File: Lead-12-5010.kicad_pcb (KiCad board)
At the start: 2 copper layers, 225.5 x 42.5 mm, 59 parts, among them U1 TL082, U2 TL082

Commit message: Removed low input
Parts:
- removed D1, D2: 1N914, Diode_THT:D_DO-35_SOD27_P7.62mm_Horizontal
- removed IN_LOW_1: IN_LOW, Audio Jacks:6.35MM_STEREO_SWITCHED_JACK
- moved H2 31.0 mm to (103.9, 127.0)
- moved IN_HIGH_1 30.0 mm to (79.8, 127.3)
- moved H5 29.3 mm to (78.6, 93.1)
- moved H4 28.1 mm to (188.1, 127.0)
- moved R4 27.7 mm to (83.6, 102.9)
- moved C3 27.7 mm to (93.7, 95.2)
- moved R5 25.0 mm to (108.8, 95.2)
- moved C4 21.6 mm to (115.2, 101.6)
- moved R6 14.9 mm to (98.7, 102.9), turned to 0 degrees
- moved H1 14.0 mm to (175.3, 93.1)
- moved Logo1 11.4 mm to (172.5, 101.7)
- moved C6 10.2 mm to (161.3, 98.7)
- moved R7 2.29 mm to (121.7, 94.0)
- moved C10 1.02 mm to (174.0, 110.2)
- moved C11 1.02 mm to (165.1, 116.6)
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- renumbered OUT to OUT1, Vcc to Vcc1
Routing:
- net /V+: track 183.0 -> 131.1 mm
- net Net-(C4-Pad2): track 45.4 -> 14.6 mm
- net Net-(C3-Pad1): track 88.8 -> 62.2 mm
- net /Vref: track 234.2 -> 219.2 mm
- net Net-(C5-Pad1): track 58.4 -> 46.0 mm
- net Net-(C6-Pad2): track 42.2 -> 32.0 mm
- net Net-(C7-Pad2): track 48.0 -> 41.0 mm
- net Net-(C5-Pad2): track 28.3 -> 26.3 mm
- net Net-(C11-Pad1): track 22.5 -> 21.5 mm
- net Net-(C11-Pad2): track 60.6 -> 61.6 mm
- net Net-(IN_HIGH_1-PadT): track 11.8 -> 12.8 mm
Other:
- board size 225.5 x 42.5 mm -> 196.1 x 42.5 mm
- board text added: "v0.2"
- board text removed: "v0.1"

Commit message: Added filter cap
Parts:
- added C19: 100u/35V, Capacitor_THT:CP_Radial_D8.0mm_P3.50mm, F.Cu at (246.1, 105.0)
- C1, C2: footprint Capacitor_THT:CP_Radial_D10.0mm_P3.50mm -> Capacitor_THT:CP_Radial_D8.0mm_P3.50mm
- C16: footprint Capacitor_THT:CP_Radial_D8.0mm_P3.50mm -> Capacitor_THT:CP_Radial_D6.3mm_P2.50mm
- moved C1 5.01 mm to (255.0, 100.3)
- moved C2 2.39 mm to (263.9, 105.0)
- moved C16 2.01 mm to (238.6, 100.3)
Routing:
- net Net-(C19-Pad1): track 14.2 -> 37.1 mm
- net /Vref: track 219.2 -> 224.0 mm
- net Net-(C16-Pad2): track 30.4 -> 33.2 mm
- net /V+: track 131.1 -> 132.6 mm
- net Net-(BOOST1-Pad2): track 51.0 -> 51.7 mm

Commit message: Preparing 0.2
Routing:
- net Net-(C19-Pad1): track 37.1 -> 37.7 mm
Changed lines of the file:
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@@
     (thickness 1.6)
     (drawings 9)
-    (tracks 284)
+    (tracks 289)
     (zones 0)
     (modules 57)
@@
   (segment (start 131.572 116.84) (end 132.461 115.951) (width 1) (layer F.Cu) (net 9))
   (segment (start 132.461 115.951) (end 139.573 115.951) (width 1) (layer F.Cu) (net 9))
-  (segment (start 263.906 105.029) (end 263.906 99.441) (width 1) (layer F.Cu) (net 9) (status 1000000))
-  (segment (start 263.906 99.441) (end 260.985 96.52) (width 1) (layer F.Cu) (net 9) (status 1000000))
-  (segment (start 260.985 96.52) (end 257.27 96.52) (width 1) (layer F.Cu) (net 9) (status 1000000))
-  (segment (start 257.27 96.52) (end 253.714 92.964) (width 1) (layer F.Cu) (net 9) (status 1000000))
-  (segment (start 253.714 92.964) (end 250.19 92.964) (width 1) (layer F.Cu) (net 9) (status 1000020))
+  (segment (start 263.906 105.029) (end 263.906 99.441) (width 1) (layer F.Cu) (net 9))
+  (segment (start 263.906 99.441) (end 260.985 96.52) (width 1) (layer F.Cu) (net 9))
+  (segment (start 260.985 96.52) (end 257.27 96.52) (width 1) (layer F.Cu) (net 9))
+  (segment (start 257.27 96.52) (end 253.714 92.964) (width 1) (layer F.Cu) (net 9))
+  (segment (start 253.714 92.964) (end 250.19 92.964) (width 1) (layer F.Cu) (net 9) (status 20))
   (segment (start 220.853 90.678) (end 220.853 92.964) (width 1) (layer F.Cu) (net 10) (status 20))
   (segment (start 220.10001 89.92501) (end 220.853 90.678) (width 1) (layer F.Cu) (net 10))
@@
   (segment (start 222.758 101.346) (end 211.709 101.346) (width 0.5) (layer B.Cu) (net 15))
   (segment (start 211.709 101.346) (end 206.502 106.553) (width 0.5) (layer B.Cu) (net 15))
-  (segment (start 229.997 102.235) (end 231.394 103.632) (width 0.5) (layer F.Cu) (net 15) (status 1000000))
-  (segment (start 229.997 101.092) (end 229.997 102.235) (width 0.5) (layer F.Cu) (net 15) (status 1000000))
-  (segment (start 231.394 103.632) (end 237.236 103.632) (width 0.5) (layer F.Cu) (net 15) (status 1000000))
-  (segment (start 237.236 103.632) (end 238.633 102.235) (width 0.5) (layer F.Cu) (net 15) (status 1000000))
-  (segment (start 238.633 102.235) (end 238.633 100.33) (width 0.5) (layer F.Cu) (net 15) (status 1000000))
+  (segment (start 229.997 102.235) (end 231.394 103.632) (width 0.5) (layer F.Cu) (net 15))
+  (segment (start 229.997 101.092) (end 229.997 102.235) (width 0.5) (layer F.Cu) (net 15))
+  (segment (start 231.394 103.632) (end 237.236 103.632) (width 0.5) (layer F.Cu) (net 15))
+  (segment (start 237.236 103.632) (end 238.633 102.235) (width 0.5) (layer F.Cu) (net 15))
+  (segment (start 238.633 102.235) (end 238.633 100.33) (width 0.5) (layer F.Cu) (net 15))
   (segment (start 151.21 97.79) (end 152.4 96.6) (width 0.5) (layer F.Cu) (net 16) (status 20))
   (segment (start 144.78 97.79) (end 151.21 97.79) (width 0.5) (layer F.Cu) (net 16) (status 10))
@@
   (segment (start 234.9 128.524) (end 236.069999 127.354001) (width 0.5) (layer F.Cu) (net 21) (status 10))
   (segment (start 236.069999 127.354001) (end 236.119999 127.354001) (width 0.5) (layer F.Cu) (net 21))
-  (segment (start 237.871 111.252) (end 237.871 107.696) (width 0.5) (layer B.Cu) (net 21) (status 1000000))
-  (segment (start 240.792 114.173) (end 237.871 111.252) (width 0.5) (layer B.Cu) (net 21) (status 1000000))
-  (segment (start 240.792 119.38) (end 240.792 114.173) (width 0.5) (layer B.Cu) (net 21) (status 1000010))
-  (segment (start 241.133 104.434) (end 237.871 107.696) (width 0.5) (layer B.Cu) (net 21) (status 1000000))
-  (segment (start 241.133 100.33) (end 241.133 104.434) (width 0.5) (layer B.Cu) (net 21) (status 1000000))
+  (segment (start 237.871 111.252) (end 237.871 107.696) (width 0.5) (layer B.Cu) (net 21))
+  (segment (start 240.792 114.173) (end 237.871 111.252) (width 0.5) (layer B.Cu) (net 21))
+  (segment (start 240.792 119.38) (end 240.792 114.173) (width 0.5) (layer B.Cu) (net 21) (status 10))
+  (segment (start 241.133 104.434) (end 237.871 107.696) (width 0.5) (layer B.Cu) (net 21))
+  (segment (start 241.133 100.33) (end 241.133 104.434) (width 0.5) (layer B.Cu) (net 21))
   (segment (start 93.137999 94.450001) (end 93.137999 94.441001) (width 0.5) (layer F.Cu) (net 22) (status 10))
   (segment (start 92.338 95.25) (end 93.137999 94.450001) (width 0.5) (layer F.Cu) (net 22) (status 20))
@@
   (segment (start 229.9 128.524) (end 229.9 124.938) (width 0.5) (layer F.Cu) (net 29) (status 10))
   (segment (start 229.9 124.938) (end 239.522 115.316) (width 0.5) (layer F.Cu) (net 29))
-  (segment (start 225.806 92.964) (end 231.013 92.964) (width 1) (layer F.Cu) (net 32) (status 20))
-  (segment (start 219.456 99.314) (end 225.806 92.964) (width 1) (layer F.Cu) (net 32) (status 10))
   (segment (start 210.121 103.314) (end 202.946 96.139) (width 1) (layer F.Cu) (net 30))
-  (segment (start 202.946 92.075) (end 200.79601 89.92501) (width 1) (layer F.Cu) (net 30))
-  (segment (start 202.946 96.139) (end 202.946 92.075) (width 1) (layer F.Cu) (net 30))
-  (segment (start 150.10499 89.92501) (end 144.78 95.25) (width 1) (layer F.Cu) (net 30) (status 20))
-  (segment (start 200.79601 89.92501) (end 150.10499 89.92501) (width 1) (layer F.Cu) (net 30))
   (segment (start 220.455999 102.314001) (end 220.455999 101.870001) (width 1) (layer F.Cu) (net 30))
   (segment (start 219.456 103.314) (end 220.455999 102.314001) (width 1) (layer F.Cu) (net 30) (status 10))
@@
   (segment (start 219.456 103.314) (end 217.234 103.314) (width 1) (layer F.Cu) (net 30) (status 10))
   (segment (start 217.234 103.314) (end 210.121 103.314) (width 1) (layer F.Cu) (net 30))
-  (segment (start 240.284 92.964) (end 243.078 95.758) (width 1) (layer B.Cu) (net 30) (status 1000000))
-  (segment (start 243.078 95.758) (end 250.063 95.758) (width 1) (layer B.Cu) (net 30) (status 1000000))
-  (segment (start 250.063 95.758) (end 254.635 100.33) (width 1) (layer B.Cu) (net 30) (status 1000000))
-  (segment (start 236.093 92.964) (end 240.284 92.964) (width 1) (layer B.Cu) (net 30) (status 1000000))
-  (segment (start 254.635 100.33) (end 255.016 100.33) (width 1) (layer B.Cu) (net 30) (status 1000000))
+  (segment (start 250.063 95.758) (end 254.635 100.33) (width 1) (layer B.Cu) (net 30))
+  (segment (start 236.093 92.964) (end 240.284 92.964) (width 1) (layer B.Cu) (net 30))
+  (segment (start 254.635 100.33) (end 255.016 100.33) (width 1) (layer B.Cu) (net 30))
+  (segment (start 202.946 96.139) (end 202.946 92.075) (width 1) (layer F.Cu) (net 30))
+  (segment (start 202.946 92.075) (end 200.79601 89.92501) (width 1) (layer F.Cu) (net 30))
+  (segment (start 150.10499 89.92501) (end 144.78 95.25) (width 1) (layer F.Cu) (net 30) (status 20))
+  (segment (start 200.79601 89.92501) (end 150.10499 89.92501) (width 1) (layer F.Cu) (net 30))
+  (segment (start 250.063 95.758) (end 250.062984 95.758) (width 1) (layer B.Cu) (net 30))
+  (segment (start 248.768985 94.464001) (end 245.110569 94.464001) (width 1) (layer B.Cu) (net 30))
+  (segment (start 250.062984 95.758) (end 248.768985 94.464001) (width 1) (layer B.Cu) (net 30))
+  (segment (start 243.610568 92.964) (end 240.284 92.964) (width 1) (layer B.Cu) (net 30))
+  (segment (start 245.110569 94.464001) (end 243.610568 92.964) (width 1) (layer B.Cu) (net 30))
   (segment (start 267.208 129.032) (end 267.208 118.411) (width 0.5) (layer F.Cu) (net 31) (status 20))
   (segment (start 265.61501 130.62499) (end 267.208 129.032) (width 0.5) (layer F.Cu) (net 31))
@@
   (segment (start 267.208 113.411) (end 265.408 113.411) (width 0.5) (layer F.Cu) (net 31) (status 10))
   (segment (start 265.408 113.411) (end 263.884 111.887) (width 0.5) (layer F.Cu) (net 31))
-  (segment (start 243.586 97.79) (end 235.839 97.79) (width 1) (layer B.Cu) (net 32) (status 1000000))
-  (segment (start 246.126 100.33) (end 243.586 97.79) (width 1) (layer B.Cu) (net 32) (status 1000000))
-  (segment (start 235.839 97.79) (end 231.013 92.964) (width 1) (layer B.Cu) (net 32) (status 1000000))
-  (segment (start 246.126 105.029) (end 246.126 100.33) (width 1) (layer B.Cu) (net 32) (status 1000000))
+  (segment (start 225.806 92.964) (end 231.013 92.964) (width 1) (layer F.Cu) (net 32) (status 20))
+  (segment (start 219.456 99.314) (end 225.806 92.964) (width 1) (layer F.Cu) (net 32) (status 10))
+  (segment (start 231.013 93.987) (end 231.013 92.964) (width 1) (layer B.Cu) (net 32))
+  (segment (start 231 94) (end 231.013 93.987) (width 1) (layer B.Cu) (net 32))
+  (segment (start 234.79 97.79) (end 231 94) (width 1) (layer B.Cu) (net 32))
+  (segment (start 243.586 97.79) (end 234.79 97.79) (width 1) (layer B.Cu) (net 32))
+  (segment (start 246.126 105.029) (end 246.126 100.33) (width 1) (layer B.Cu) (net 32))
+  (segment (start 246.126 100.33) (end 243.586 97.79) (width 1) (layer B.Cu) (net 32))
   (zone (net 3) (net_name GND) (layer B.Cu) (hatch edge 0.508)
     (connect_pads (clearance 0.2))
@@
     (polygon
       (pts
-        (xy 73.279 88.138) (xy 270.51 87.63) (xy 270.51 132.08) (xy 73.279 132.588)
+        (xy 73.279 88.138) (xy 271 87.775) (xy 271 132.225) (xy 73.279 132.588)
       )
     )

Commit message: 3D Path
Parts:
- moved L1 0.64 mm to (219.5, 99.9)
- moved Vcc1 0.38 mm to (207.6, 93.0)
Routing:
- net Net-(BOOST1-Pad1): track 46.9 -> 47.6 mm
- net Net-(C19-Pad1): track 37.7 -> 38.3 mm
- net /Vcc: track 18.0 -> 18.6 mm
- net Net-(BOOST1-Pad2): track 51.7 -> 51.2 mm

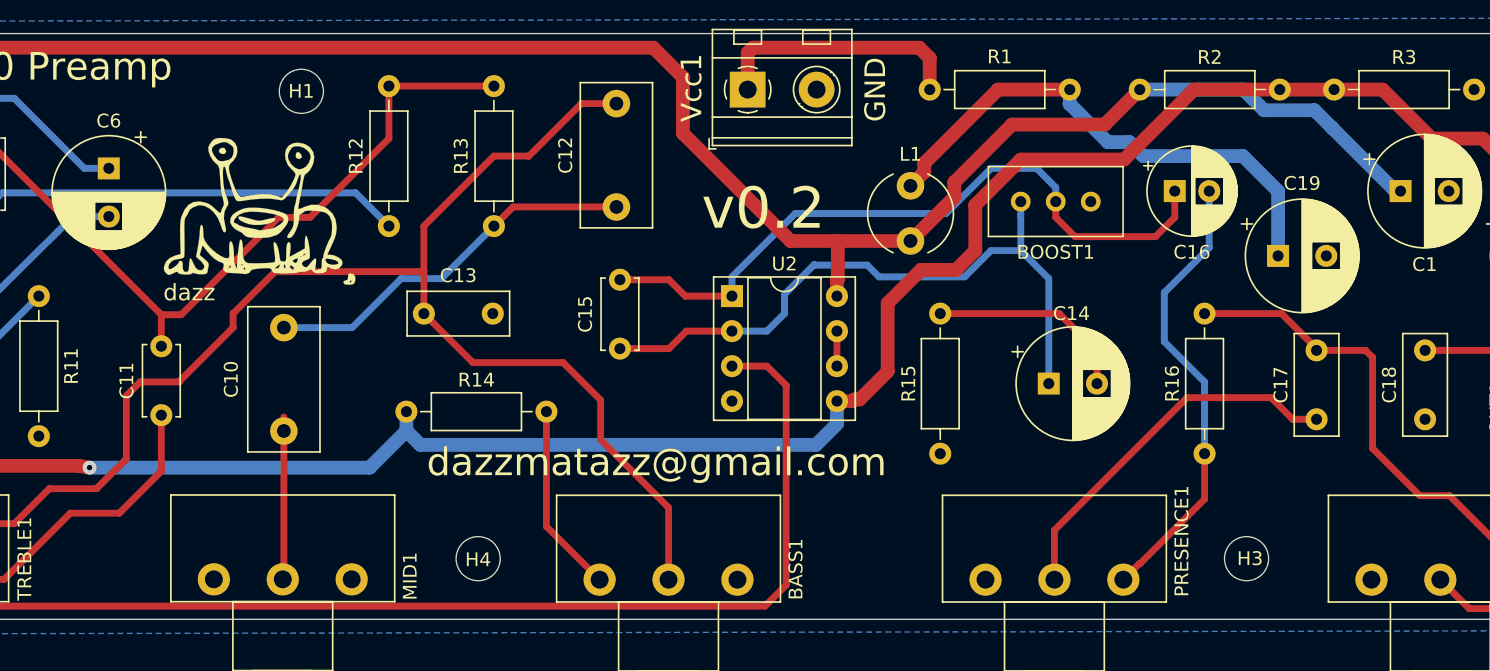
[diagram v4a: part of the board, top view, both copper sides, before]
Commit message: Changed output buffer to BJT, removed op amp booster
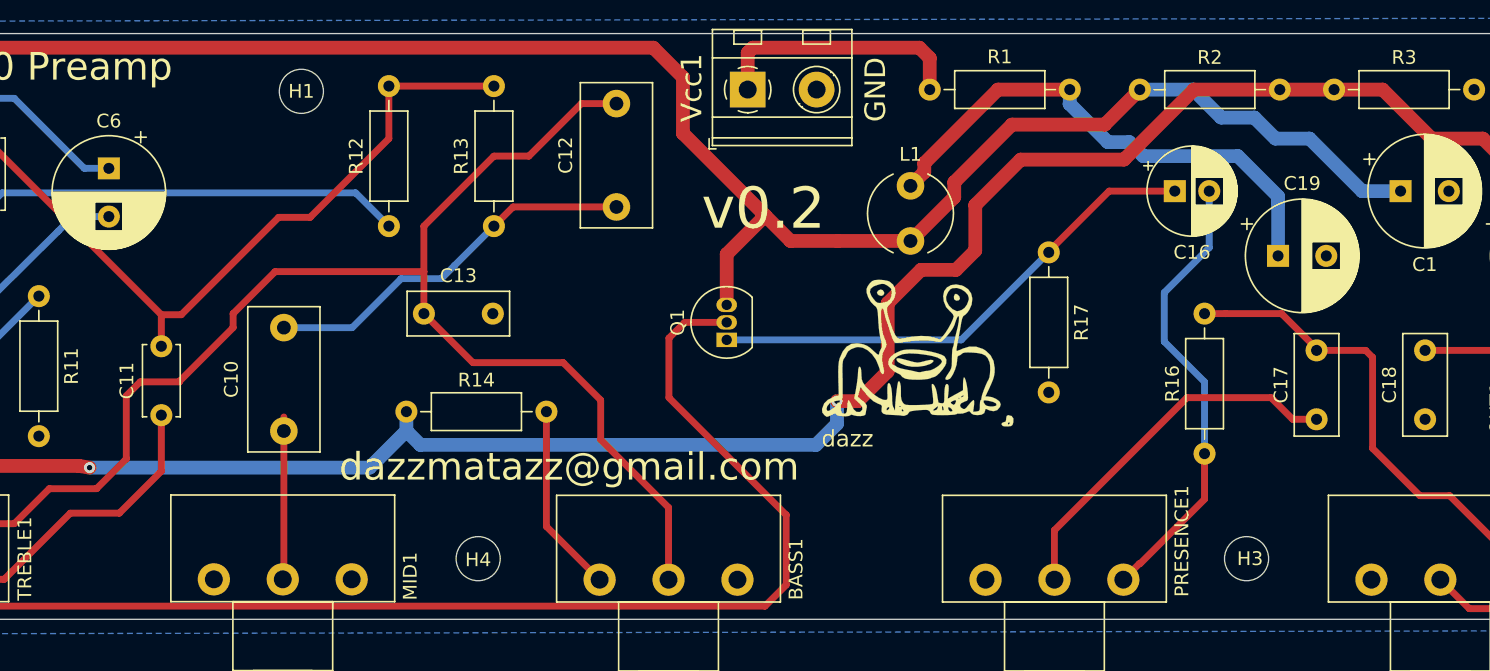
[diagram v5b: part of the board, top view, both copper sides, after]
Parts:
- removed BOOST1: 25K, Potentiometer_THT:Potentiometer_Bourns_3296W_Vertical
- removed C14: 47u, Capacitor_THT:CP_Radial_D8.0mm_P3.50mm
- removed C15: 220p, Capacitor_THT:C_Disc_D5.0mm_W2.5mm_P5.00mm
- removed R15: 1K, Resistor_THT:R_Axial_DIN0207_L6.3mm_D2.5mm_P10.16mm_Horizontal
- removed U2: TL082, Package_DIP:DIP-8_W7.62mm_Socket
- added Q1: 2N3904, Package_TO_SOT_THT:TO-92_Inline, F.Cu at (206.1, 111.1)
- added R17: 33k, Resistor_THT:R_Axial_DIN0207_L6.3mm_D2.5mm_P10.16mm_Horizontal, F.Cu at (229.5, 104.8)
- L1: value 5m -> 5mH
- moved Logo1 48.8 mm to (220.2, 112.0)
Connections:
- net /Vref renamed Vref
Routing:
- net Net-(BOOST1-Pad1): track 47.6 -> 0.00 mm
- net Net-(C14-Pad2): track 14.9 -> 0.00 mm
- net Net-(C16-Pad1): track 51.2 -> 37.0 mm
- net Net-(Q1-Pad2): track 85.0 -> 92.1 mm
- net /V+: track 132.9 -> 136.9 mm
- net Net-(U2-Pad6): track 2.54 -> 0.00 mm
- net Vref: vias 1 -> 2
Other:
- net class Default: clearance 0.5 -> 0.2
- net class PWR: clearance 0.2 -> 0.5; via_dia 1 -> 0.8
- rule trace_clearance: 0.5 -> 0.2

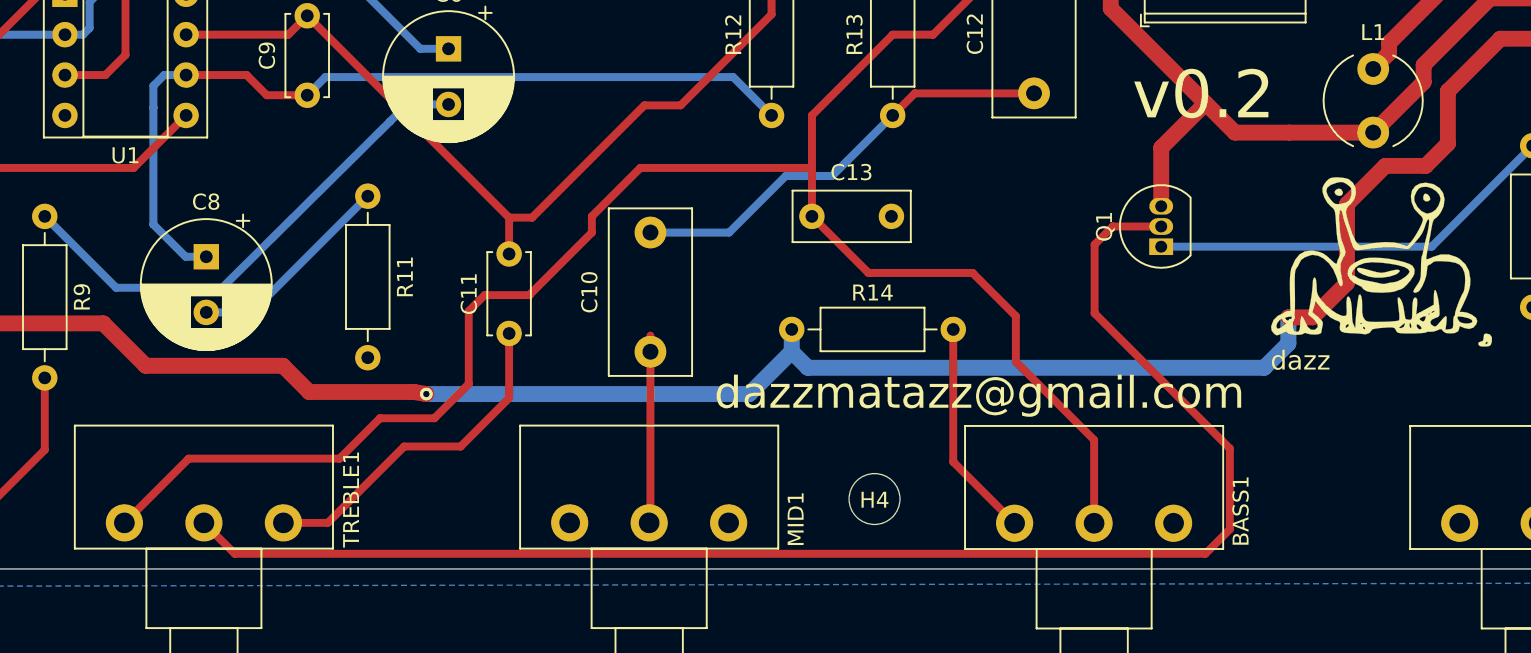
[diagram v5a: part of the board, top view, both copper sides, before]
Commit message: New transistor footprint
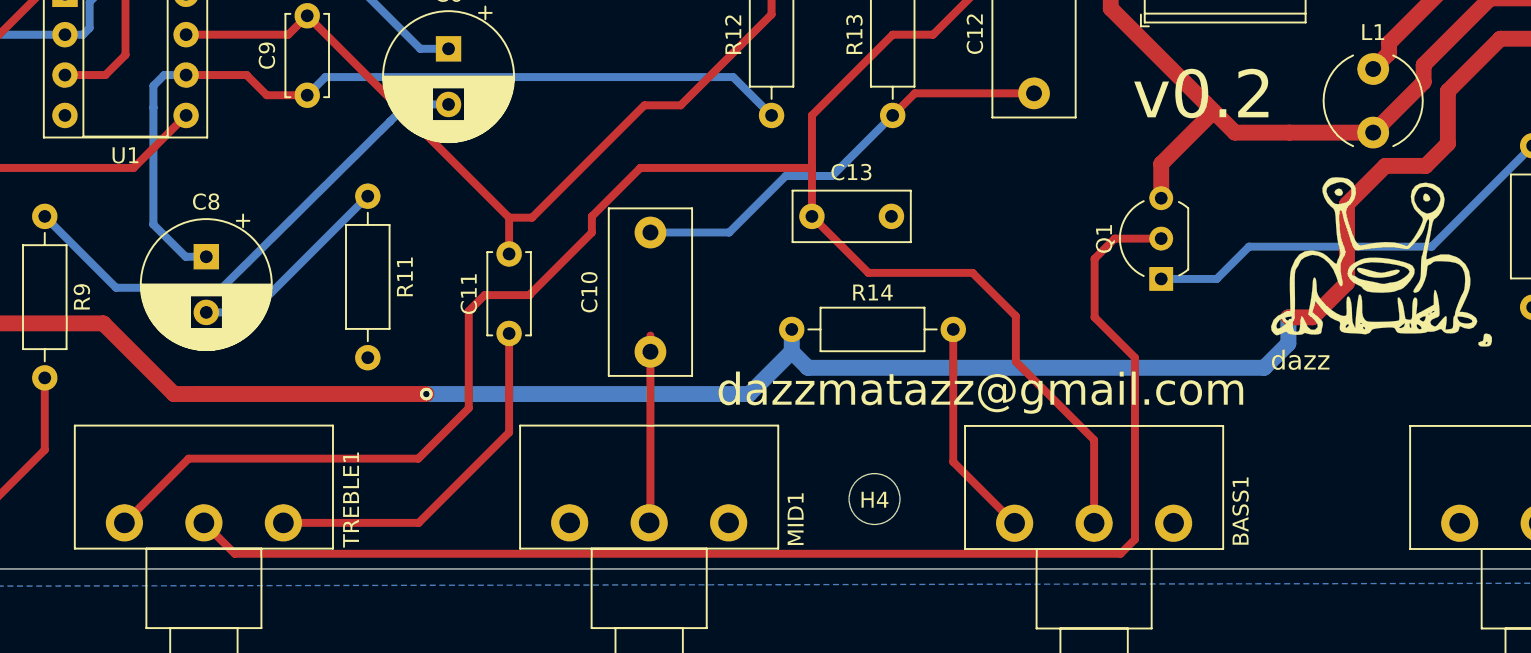
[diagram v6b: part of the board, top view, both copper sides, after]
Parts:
- Q1: footprint Package_TO_SOT_THT:TO-92_Inline -> Package_TO_SOT_THT:TO-92L_Inline_Wide
- moved Q1 2.03 mm to (206.1, 113.2)
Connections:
- net /V+ renamed V+
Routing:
- net Net-(Q1-Pad2): track 92.1 -> 83.2 mm
- net Net-(C11-Pad1): track 21.5 -> 22.8 mm
- net Net-(BASS1-Pad2): track 110.3 -> 111.2 mm
- net Net-(C16-Pad1): track 37.0 -> 37.9 mm
- net V+: track 136.9 -> 136.1 mm
